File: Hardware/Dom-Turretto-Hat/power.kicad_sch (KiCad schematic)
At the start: 26 parts

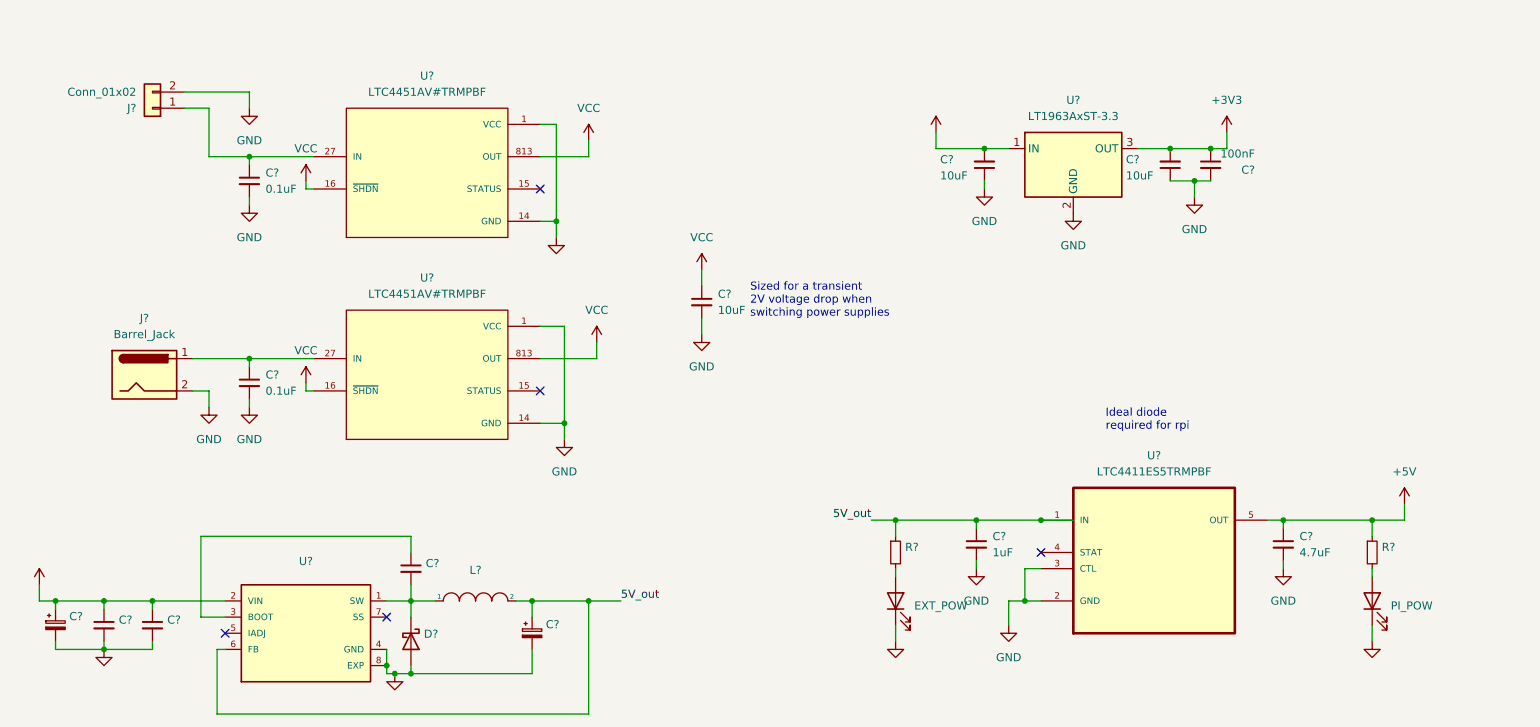
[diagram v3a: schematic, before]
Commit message: Assigned footprints
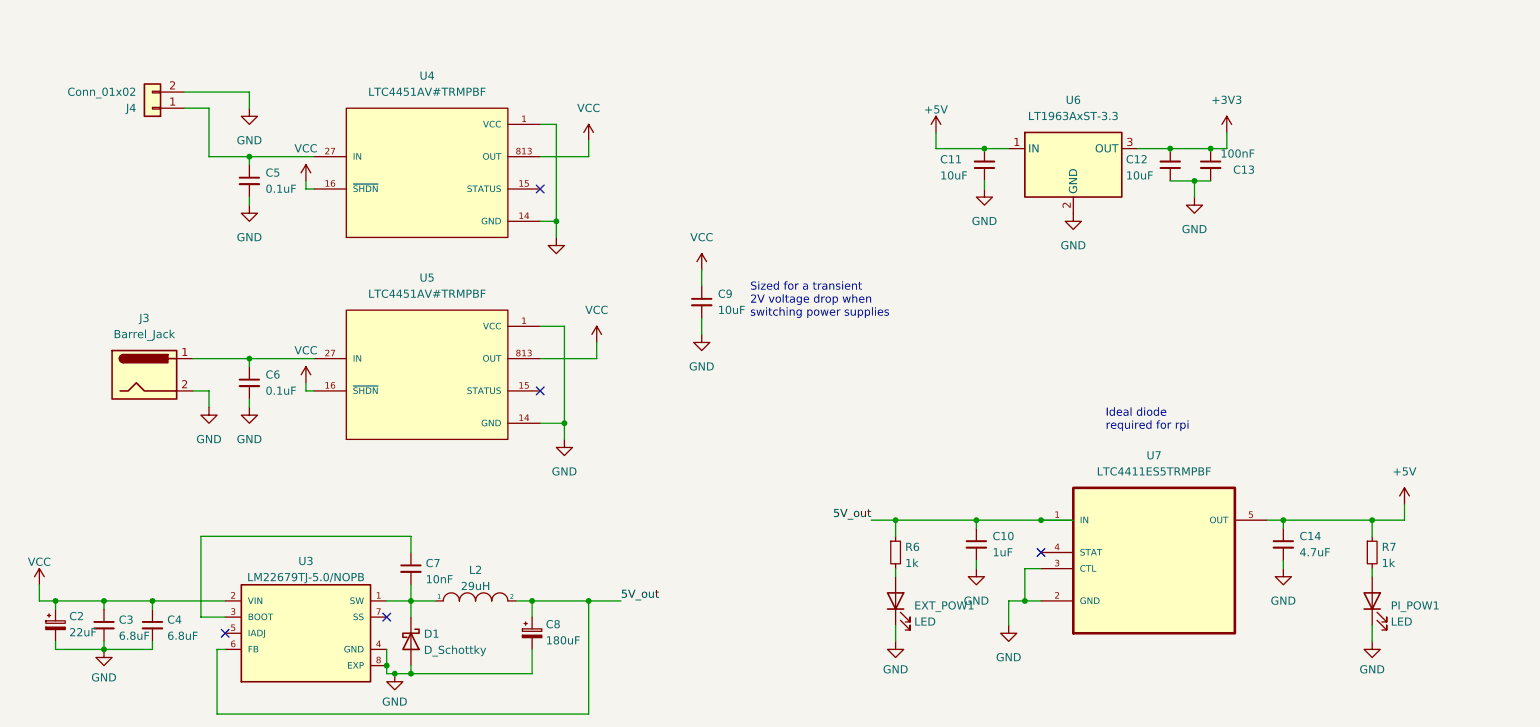
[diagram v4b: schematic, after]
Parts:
- C2: renamed from C?; value (none) -> 22uF
- C3, C4: renamed from C?; value (none) -> 6.8uF
- C7: renamed from C?; value (none) -> 10nF
- C8: renamed from C?; value (none) -> 180uF
- D1: renamed from D?; value (none) -> D_Schottky
- EXT_POW1: renamed from EXT_POW; value (none) -> LED
- L2: renamed from L?; value (none) -> 29uH
- PI_POW1: renamed from PI_POW; value (none) -> LED
- R6, R7: renamed from R?; value (none) -> 1k
- U3: renamed from U?; value (none) -> LM22679TJ-5.0/NOPB
- U4, U5: renamed from U?; footprint IC_LTC4451AV#TRMPBF -> (none)
- gave numbers to parts that had none: 12

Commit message: Made initial layout
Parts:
- removed J3: Barrel_Jack, symbol Connector:Barrel_Jack
- added J3: (no value), symbol Connector:Barrel_Jack_Switch
- C2, C3, C4, C5, C6, C7, C9: footprint (none) -> Capacitor_SMD:C_0603_1608Metric
- C8: footprint (none) -> Capacitor_SMD:CP_Elec_8x11.9
- D1: footprint (none) -> Diode_SMD:D_SOD-123
- EXT_POW1, PI_POW1: footprint (none) -> LED_SMD:LED_0603_1608Metric
- J4: footprint (none) -> Connector_AMASS:AMASS_XT60-F_1x02_P7.20mm_Vertical
- L2: footprint (none) -> Inductor_SMD:L_12x12mm_H8mm
- R6, R7: footprint (none) -> Resistor_SMD:R_0603_1608Metric
- U3: footprint (none) -> iclr:TO127P1401X200-7N
- U4, U5: footprint (none) -> iclr:IC_LTC4451AV#TRMPBF
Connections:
- net GND: now also J3.2
- net at C6.1, U5.27 (IN): now also J3.1
- no-connect marks 5 -> 6
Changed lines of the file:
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@@
   (no_connect (at 119.38 99.06))
   (no_connect (at 95.25 134.62))
+  (no_connect (at 64.77 96.52))
   (no_connect (at 69.85 137.16))
   (wire (pts (xy 193.04 132.08) (xy 195.58 132.08))
@@
     (property "Reference" "U3" (id 0) (at 82.55 125.8402 0))
     (property "Value" "LM22679TJ-5.0{slash}NOPB" (id 1) (at 82.55 128.3771 0))
-    (property "Footprint" "" (id 2) (at 82.55 137.16 0)
+    (property "Footprint" "iclr:TO127P1401X200-7N" (id 2) (at 82.55 137.16 0)
       (effects (font (size 1.27 1.27)) (justify left bottom) hide)
     )
@@
       (effects (font (size 1.27 1.27)) (justify left))
     )
-    (property "Footprint" "" (id 2) (at 99.06 127 0)
+    (property "Footprint" "Capacitor_SMD:C_0603_1608Metric" (id 2) (at 99.06 127 0)
       (effects (font (size 1.27 1.27)) hide)
     )
@@
       (effects (font (size 1.27 1.27)) (justify right))
     )
-    (property "Footprint" "" (id 2) (at 175.26 132.08 0)
+    (property "Footprint" "LED_SMD:LED_0603_1608Metric" (id 2) (at 175.26 132.08 0)
       (effects (font (size 1.27 1.27)) hide)
     )
@@
       (effects (font (size 1.27 1.27)) (justify left))
     )
-    (property "Footprint" "" (id 2) (at 144.78 85.09 0)
+    (property "Footprint" "Capacitor_SMD:C_0603_1608Metric" (id 2) (at 144.78 85.09 0)
       (effects (font (size 1.27 1.27)) hide)
     )
@@
       (effects (font (size 1.27 1.27)) (justify left))
     )
-    (property "Footprint" "" (id 2) (at 73.66 97.79 0)
+    (property "Footprint" "Capacitor_SMD:C_0603_1608Metric" (id 2) (at 73.66 97.79 0)
       (effects (font (size 1.27 1.27)) hide)
     )
@@
       (effects (font (size 1.27 1.27)) (justify right))
     )
-    (property "Footprint" "" (id 2) (at 250.19 132.08 0)
+    (property "Footprint" "LED_SMD:LED_0603_1608Metric" (id 2) (at 250.19 132.08 0)
       (effects (font (size 1.27 1.27)) hide)
     )
@@
     (property "Reference" "U4" (id 0) (at 101.6 49.53 0))
     (property "Value" "LTC4451AV#TRMPBF" (id 1) (at 101.6 52.07 0))
-    (property "Footprint" "" (id 2) (at 101.6 64.77 0)
+    (property "Footprint" "iclr:IC_LTC4451AV#TRMPBF" (id 2) (at 101.6 64.77 0)
       (effects (font (size 1.27 1.27)) (justify left bottom) hide)
     )
@@
       (effects (font (size 1.27 1.27)) (justify left))
     )
-    (property "Footprint" "" (id 2) (at 118.11 137.16 0)
+    (property "Footprint" "Capacitor_SMD:CP_Elec_8x11.9" (id 2) (at 118.11 137.16 0)
       (effects (font (size 1.27 1.27)) hide)
     )
@@
       (effects (font (size 1.27 1.27)) (justify left))
     )
-    (property "Footprint" "" (id 2) (at 58.42 135.89 0)
+    (property "Footprint" "Capacitor_SMD:C_0603_1608Metric" (id 2) (at 58.42 135.89 0)
       (effects (font (size 1.27 1.27)) hide)
     )
@@
     (property "Reference" "L2" (id 0) (at 109.22 127.2372 0))
     (property "Value" "29uH" (id 1) (at 109.22 129.7741 0))
-    (property "Footprint" "" (id 2) (at 109.22 132.08 0)
+    (property "Footprint" "Inductor_SMD:L_12x12mm_H8mm" (id 2) (at 109.22 132.08 0)
       (effects (font (size 1.27 1.27)) hide)
     )
@@
       (effects (font (size 1.27 1.27)) (justify left))
     )
-    (property "Footprint" "" (id 2) (at 99.06 138.43 0)
+    (property "Footprint" "Diode_SMD:D_SOD-123" (id 2) (at 99.06 138.43 0)
       (effects (font (size 1.27 1.27)) hide)
     )
@@
       (effects (font (size 1.27 1.27)) (justify left))
     )
-    (property "Footprint" "" (id 2) (at 58.42 54.61 0)
+    (property "Footprint" "Connector_AMASS:AMASS_XT60-F_1x02_P7.20mm_Vertical" (id 2) (at 58.42 54.61 0)
       (effects (font (size 1.27 1.27)) hide)
     )
@@
       (effects (font (size 1.27 1.27)) (justify left))
     )
-    (property "Footprint" "" (id 2) (at 50.8 135.89 0)
+    (property "Footprint" "Capacitor_SMD:C_0603_1608Metric" (id 2) (at 50.8 135.89 0)
       (effects (font (size 1.27 1.27)) hide)
     )
@@
     (property "Reference" "U5" (id 0) (at 101.6 81.28 0))
     (property "Value" "LTC4451AV#TRMPBF" (id 1) (at 101.6 83.82 0))
-    (property "Footprint" "" (id 2) (at 101.6 96.52 0)
+    (property "Footprint" "iclr:IC_LTC4451AV#TRMPBF" (id 2) (at 101.6 96.52 0)
       (effects (font (size 1.27 1.27)) (justify left bottom) hide)
     )
@@
     (pin "1")
   )
+  (symbol (lib_id "Connector:Barrel_Jack_Switch") (at 57.15 96.52 0) (unit 1)
+    (in_bom yes) (on_board yes) (fields_autoplaced)
+    (property "Reference" "J3" (id 0) (at 57.15 89.0102 0))
+    (property "Value" "" (id 1) (at 57.15 91.5471 0))
+    (property "Footprint" "" (id 2) (at 58.42 97.536 0)
+      (effects (font (size 1.27 1.27)) hide)
+    )
+    (property "Datasheet" "~" (id 3) (at 58.42 97.536 0)
+      (effects (font (size 1.27 1.27)) hide)
+    )
+    (pin "1")
+    (pin "2")
+    (pin "3")
+  )
   (symbol (lib_id "Device:R_Small") (at 250.19 124.46 0) (unit 1)
     (in_bom yes) (on_board yes) (fields_autoplaced)
@@
       (effects (font (size 1.27 1.27)) (justify left))
     )
-    (property "Footprint" "" (id 2) (at 250.19 124.46 0)
+    (property "Footprint" "Resistor_SMD:R_0603_1608Metric" (id 2) (at 250.19 124.46 0)
       (effects (font (size 1.27 1.27)) hide)
     )
@@
       (effects (font (size 1.27 1.27)) (justify left))
     )
-    (property "Footprint" "" (id 2) (at 43.18 135.89 0)
+    (property "Footprint" "Capacitor_SMD:C_0603_1608Metric" (id 2) (at 43.18 135.89 0)
       (effects (font (size 1.27 1.27)) hide)
     )
@@
     (pin "1")
   )
-  (symbol (lib_id "Connector:Barrel_Jack") (at 57.15 96.52 0) (unit 1)
-    (in_bom yes) (on_board yes) (fields_autoplaced)
-    (property "Reference" "J3" (id 0) (at 57.15 87.63 0))
-    (property "Value" "Barrel_Jack" (id 1) (at 57.15 90.17 0))
-    (property "Footprint" "" (id 2) (at 58.42 97.536 0)
-      (effects (font (size 1.27 1.27)) hide)
-    )
-    (property "Datasheet" "~" (id 3) (at 58.42 97.536 0)
-      (effects (font (size 1.27 1.27)) hide)
-    )
-    (pin "1")
-    (pin "2")
-  )
   (symbol (lib_id "Device:C_Small") (at 73.66 66.04 0) (unit 1)
     (in_bom yes) (on_board yes) (fields_autoplaced)
@@
       (effects (font (size 1.27 1.27)) (justify left))
     )
-    (property "Footprint" "" (id 2) (at 73.66 66.04 0)
+    (property "Footprint" "Capacitor_SMD:C_0603_1608Metric" (id 2) (at 73.66 66.04 0)
       (effects (font (size 1.27 1.27)) hide)
     )
@@
       (effects (font (size 1.27 1.27)) (justify left))
     )
-    (property "Footprint" "" (id 2) (at 175.26 124.46 0)
-      (effects (font (size 1.27 1.27)) hide)
-    )
+    (property "Footprint" "Resistor_SMD:R_0603_1608Metric" (id 2) (at 175.26 124.46 0)
+      (effects (font (size 1.27 1.27)) hide)
+    )

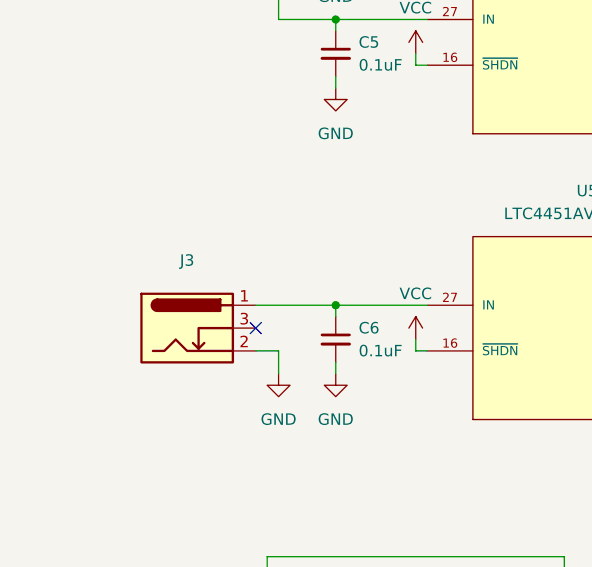
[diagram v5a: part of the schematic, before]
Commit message: Fix XT60 connector
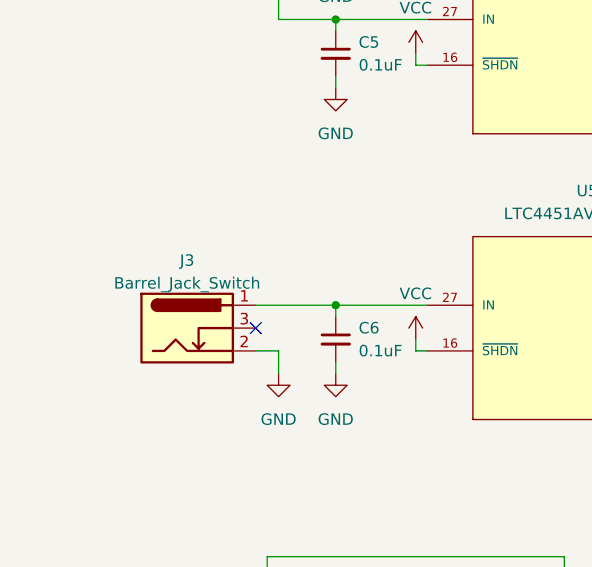
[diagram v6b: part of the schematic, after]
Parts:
- J3: value (none) -> Barrel_Jack_Switch; footprint (none) -> Connector_BarrelJack:BarrelJack_Wuerth_6941xx301002
- J4: footprint Connector_AMASS:AMASS_XT60-F_1x02_P7.20mm_Vertical -> (none)
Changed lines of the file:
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@@
       (effects (font (size 1.27 1.27)) (justify left))
     )
-    (property "Footprint" "Connector_AMASS:AMASS_XT60-F_1x02_P7.20mm_Vertical" (id 2) (at 58.42 54.61 0)
+    (property "Footprint" "" (id 2) (at 58.42 54.61 0)
       (effects (font (size 1.27 1.27)) hide)
     )
@@
     (in_bom yes) (on_board yes) (fields_autoplaced)
     (property "Reference" "J3" (id 0) (at 57.15 89.0102 0))
-    (property "Value" "" (id 1) (at 57.15 91.5471 0))
-    (property "Footprint" "" (id 2) (at 58.42 97.536 0)
+    (property "Value" "Barrel_Jack_Switch" (id 1) (at 57.15 91.5471 0))
+    (property "Footprint" "Connector_BarrelJack:BarrelJack_Wuerth_6941xx301002" (id 2) (at 58.42 97.536 0)
       (effects (font (size 1.27 1.27)) hide)
     )

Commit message: Updated schematic
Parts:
- J4: footprint (none) -> Connector_AMASS:AMASS_XT60-M_1x02_P7.20mm_Vertical
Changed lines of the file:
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@@
       (effects (font (size 1.27 1.27)) (justify left))
     )
-    (property "Footprint" "" (id 2) (at 58.42 54.61 0)
+    (property "Footprint" "Connector_AMASS:AMASS_XT60-M_1x02_P7.20mm_Vertical" (id 2) (at 58.42 54.61 0)
       (effects (font (size 1.27 1.27)) hide)
     )

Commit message: Update components
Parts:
- removed U4, U5: LTC4451AV#TRMPBF, iclr:IC_LTC4451AV#TRMPBF, symbol iclr:LTC4451AV#TRMPBF
- added Q1, Q2: RSJ250P10TL, Package_TO_SOT_SMD:TO-263-3_TabPin2, symbol iclr:RSJ250P10TL
- added R4: 470k, Resistor_SMD:R_0603_1608Metric, symbol Device:R_Small
- added U2: LTC4412xS6, Package_TO_SOT_SMD:TSOT-23-6, symbol Power_Management:LTC4412xS6
- J4: footprint Connector_AMASS:AMASS_XT60-M_1x02_P7.20mm_Vertical -> Connector_AMASS:AMASS_XT60-F_1x02_P7.20mm_Vertical
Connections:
- net GND: now also U2.2 (GND), U2.3 (CTL)
- net VCC: now also Q1.3, Q2.3, R4.2, U2.6 (SENSE)
- net at C6.1, J3.1: now also Q2.2
- net at C5.1, J4.1 (Pin_1): now also Q1.2, U2.1 (VIN)
- new net: Q2.1, R4.1, U2.4 (STAT)
- new net: Q1.1, U2.5 (GATE)
- no-connect marks 6 -> 4
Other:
- moved on the sheet: C5, C6, J3, J4
